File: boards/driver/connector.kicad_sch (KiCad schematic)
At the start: 1 part, among them J1 DIN41612_03x32_C

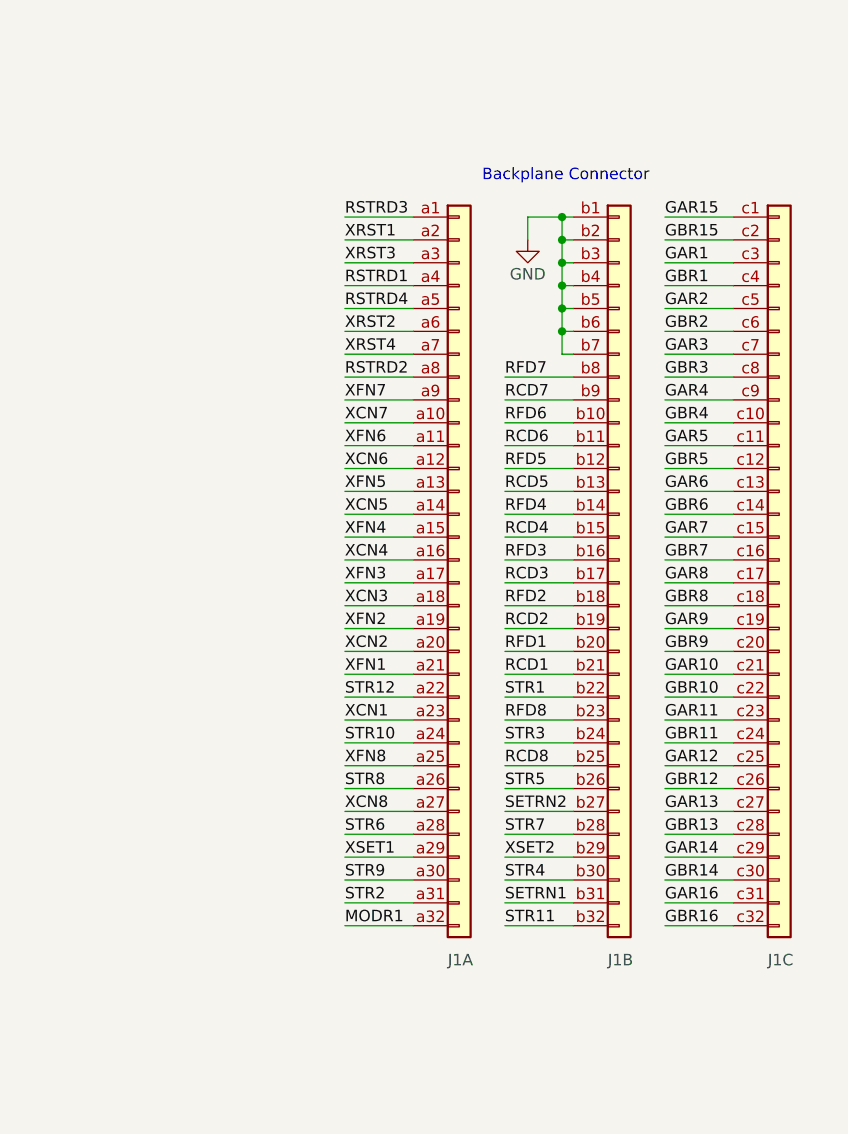
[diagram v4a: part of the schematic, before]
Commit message: Driver: routed a few more signals and annotated net equivalent names for the rope connector
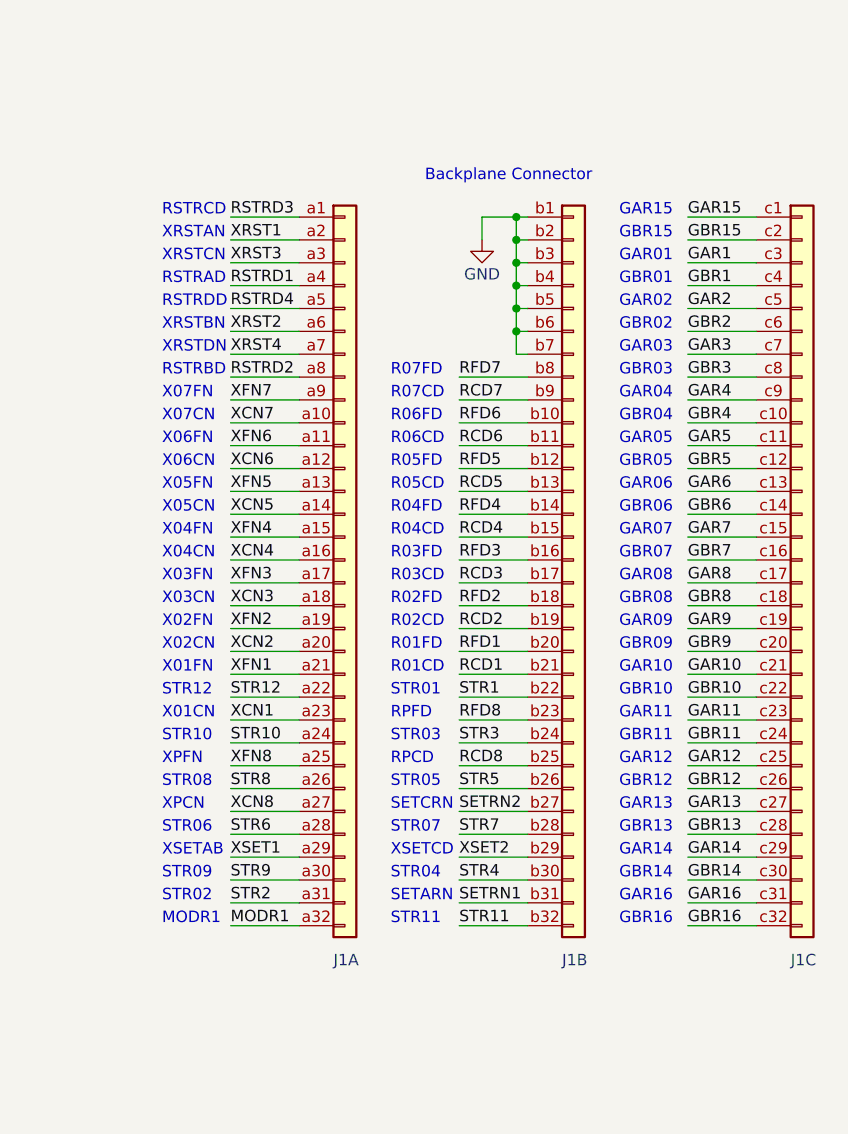
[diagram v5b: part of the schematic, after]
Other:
- note added: "GAR01"
- note added: "GAR02"
- note added: "GAR03"
- note added: "GAR04"
- note added: "GAR05"
- note added: "GAR06"
- note added: "GAR07"
- note added: "GAR08"
- note added: "GAR09"
- note added: "GAR10"
- note added: "GAR11"
- note added: "GAR12"
- note added: "GAR13"
- note added: "GAR14"
- note added: "GAR15"
- note added: "GAR16"
- note added: "GBR01"
- note added: "GBR02"
- note added: "GBR03"
- note added: "GBR04"
- note added: "GBR05"
- note added: "GBR06"
- note added: "GBR07"
- note added: "GBR08"
- note added: "GBR09"
- note added: "GBR10"
- note added: "GBR11"
- note added: "GBR12"
- note added: "GBR13"
- note added: "GBR14"
- note added: "GBR15"
- note added: "GBR16"
- note added: "MODR1"
- note added: "R01CD"
- note added: "R01FD"
- note added: "R02CD"
- note added: "R02FD"
- note added: "R03CD"
- note added: "R03FD"
- note added: "R04CD"
- note added: "R04FD"
- note added: "R05CD"
- note added: "R05FD"
- note added: "R06CD"
- note added: "R06FD"
- note added: "R07CD"
- note added: "R07FD"
- note added: "RPCD"
- note added: "RPFD"
- note added: "RSTRAD"
- note added: "RSTRBD"
- note added: "RSTRCD"
- note added: "RSTRDD"
- note added: "SETARN"
- note added: "SETCRN"
- note added: "STR01"
- note added: "STR02"
- note added: "STR03"
- note added: "STR04"
- note added: "STR05"
- note added: "STR06"
- note added: "STR07"
- note added: "STR08"
- note added: "STR09"
- note added: "STR10"
- note added: "STR11"
- note added: "STR12"
- note added: "X01CN"
- note added: "X01FN"
- note added: "X02CN"
- note added: "X02FN"
- note added: "X03CN"
- note added: "X03FN"
- note added: "X04CN"
- note added: "X04FN"
- note added: "X05CN"
- note added: "X05FN"
- note added: "X06CN"
- note added: "X06FN"
- note added: "X07CN"
- note added: "X07FN"
- note added: "XPCN"
- note added: "XPFN"
- note added: "XRSTAN"
- note added: "XRSTBN"
- note added: "XRSTCN"
- note added: "XRSTDN"
- note added: "XSETAB"
- note added: "XSETCD"
- moved on the sheet: J1A, J1B, J1C

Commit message: Driver: minor schematic cleanup and populated all of the BOM except for resistors
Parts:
- J1: Notes (none) -> DNP
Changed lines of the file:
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@@
+      (effects (font (size 1.27 1.27)) hide)
+    )
+    (property "Notes" "DNP" (id 4) (at 173.99 80.01 0)
       (effects (font (size 1.27 1.27)) hide)
     )
@@
       (effects (font (size 1.27 1.27)) hide)
     )
+    (property "Notes" "DNP" (id 4) (at 199.39 80.01 0)
+      (effects (font (size 1.27 1.27)) hide)
+    )
     (pin "a1")
     (pin "a10")
@@
       (effects (font (size 1.27 1.27)) hide)
     )
+    (property "Notes" "DNP" (id 4) (at 224.79 80.01 0)
+      (effects (font (size 1.27 1.27)) hide)
+    )

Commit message: Driver: corrected reference divider resistor and added diode direction symbols to the silkscreen
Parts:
- J1: MPN (none) -> 86093967113755ELF; Manufacturer (none) -> Amphenol ICC (FCI)
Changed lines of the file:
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@@
+      (effects (font (size 1.27 1.27)) hide)
+    )
+    (property "Description" "CONN DIN HDR 96POS PCB RA GOLD" (id 5) (at 173.99 80.01 0)
+      (effects (font (size 1.27 1.27)) hide)
+    )
+    (property "MPN" "86093967113755ELF" (id 6) (at 173.99 80.01 0)
+      (effects (font (size 1.27 1.27)) hide)
+    )
+    (property "Manufacturer" "Amphenol ICC (FCI)" (id 7) (at 173.99 80.01 0)
       (effects (font (size 1.27 1.27)) hide)
     )
@@
       (effects (font (size 1.27 1.27)) hide)
     )
+    (property "Description" "CONN DIN HDR 96POS PCB RA GOLD" (id 5) (at 199.39 80.01 0)
+      (effects (font (size 1.27 1.27)) hide)
+    )
+    (property "MPN" "86093967113755ELF" (id 6) (at 199.39 80.01 0)
+      (effects (font (size 1.27 1.27)) hide)
+    )
+    (property "Manufacturer" "Amphenol ICC (FCI)" (id 7) (at 199.39 80.01 0)
+      (effects (font (size 1.27 1.27)) hide)
+    )
     (pin "a1")
     (pin "a10")
@@
       (effects (font (size 1.27 1.27)) hide)
     )
+    (property "Description" "CONN DIN HDR 96POS PCB RA GOLD" (id 5) (at 224.79 80.01 0)
+      (effects (font (size 1.27 1.27)) hide)
+    )
+    (property "MPN" "86093967113755ELF" (id 6) (at 224.79 80.01 0)
+      (effects (font (size 1.27 1.27)) hide)
+    )
+    (property "Manufacturer" "Amphenol ICC (FCI)" (id 7) (at 224.79 80.01 0)
+      (effects (font (size 1.27 1.27)) hide)
+    )
